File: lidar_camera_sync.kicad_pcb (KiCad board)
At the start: 2 copper layers, 64 parts, among them J1 SWD, J2 XLB16PW-M, J3 XLB16PW-M, J4 BM08B-GHS-TBT(LF)(SN), J5 Pinheader_4P, SW1 TS-1088-AR02016, U1 STM32G431KBUx, U2 TPS54560DDAR, U3 RT9013-33GB, U4 AMS1117-5.0, U5 MAX3232ESE+T, U6 ISO7720D, Y1 X32258MOB4SI

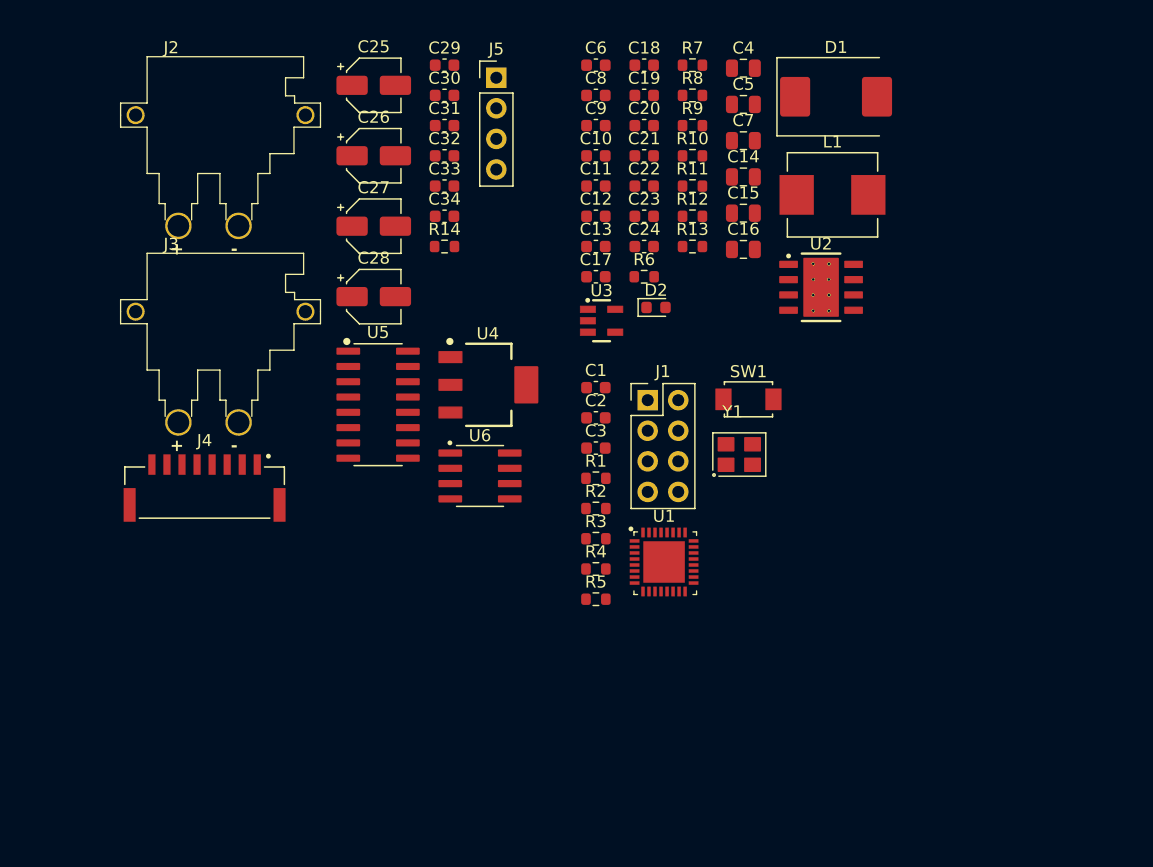
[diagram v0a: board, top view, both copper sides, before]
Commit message: [Modify]: 修复一些封装错误, 完成基本Layout器件摆放
JIRA-ID: N/A

修复一些封装错误, 完成基本Layout器件摆放
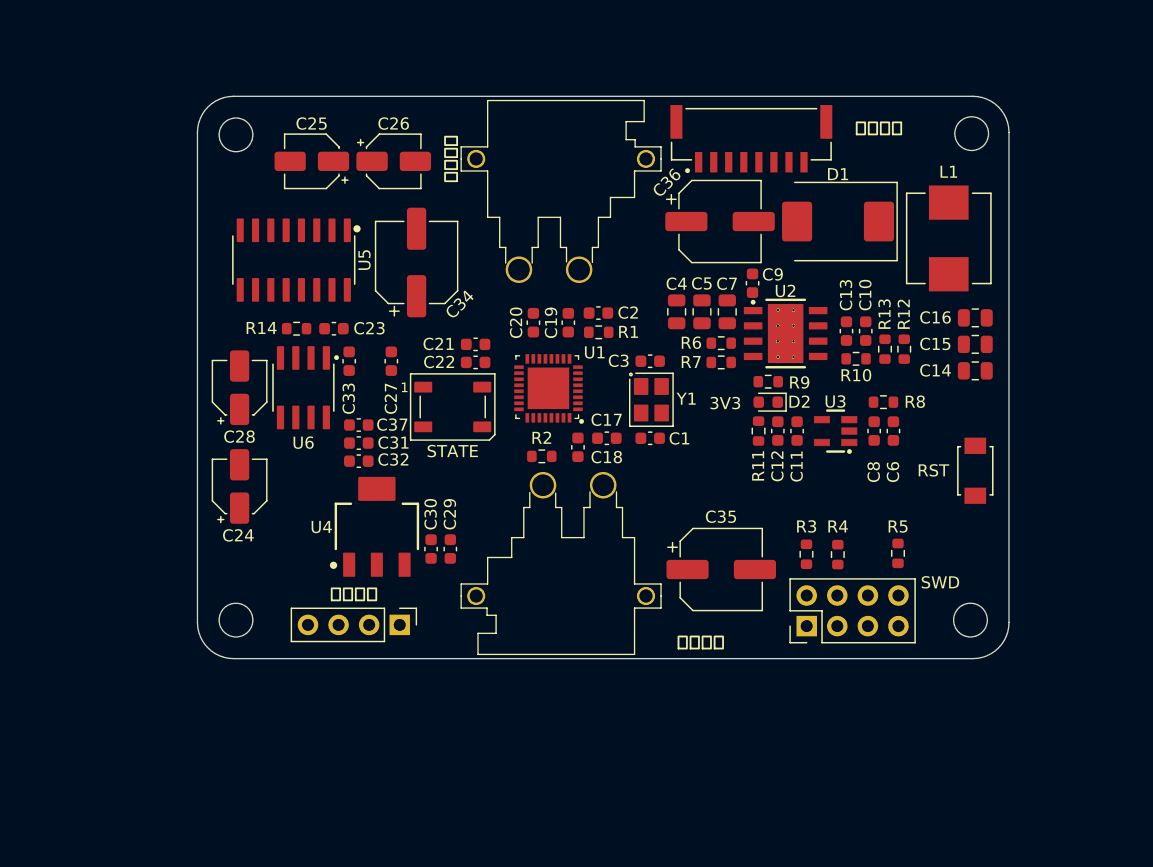
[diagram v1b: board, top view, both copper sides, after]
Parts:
- removed the C24 at (138.5, 94.4)
- added C27: 100nF, Capacitor_SMD:C_0603_1608Metric, F.Cu at (117.5, 103.9)
- added C34: 22uF, Capacitor_SMD:CP_Elec_6.3x5.4, F.Cu at (119.6, 95.7)
- added C35: 22uF, Capacitor_SMD:CP_Elec_6.3x5.4, F.Cu at (144.9, 121.2)
- added C36: 22uF, Capacitor_SMD:CP_Elec_6.3x5.4, F.Cu at (144.8, 92.3)
- added STATE: WS2812B, LED_SMD:LED_WS2812B_PLCC4_5.0x5.0mm_P3.2mm, F.Cu at (122.6, 107.7)
- SWD: renamed from J1; footprint Connector_PinHeader_2.54mm:PinHeader_2x04_P2.54mm_Vertical -> lidar_camera_sync:Pinheader_2x04_P2.54mm
- moved J4 55.4 mm to (147.4, 84.0), turned to 180 degrees
- moved 雷达接口 46.1 mm to (118.2, 125.8), turned to -90 degrees
- moved C29 40.2 mm to (122.4, 119.5), turned to 90 degrees
- moved C6 39.2 mm to (159.2, 109.7), turned to 90 degrees
- moved C30 37.7 mm to (120.8, 119.5), turned to 90 degrees
- moved 雷达电源 36.8 mm to (131.6, 123.4), turned to 180 degrees
- moved C8 36.2 mm to (157.6, 109.7), turned to 90 degrees
- moved C24 35.1 mm to (104.9, 114.3), turned to 90 degrees
- moved C18 32.2 mm to (133.0, 111.0), turned to -90 degrees
- moved R8 30.0 mm to (158.4, 107.3)
- moved 相机电源 28.5 mm to (131.6, 87.1)
- moved C23 27.4 mm to (112.7, 101.2), turned to 180 degrees
- moved C31 27.3 mm to (114.8, 110.7)
- moved C10 26.7 mm to (156.9, 101.4), turned to 90 degrees
- moved C32 26.3 mm to (114.8, 112.2)
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- renumbered C25 to C24, C26 to C25, C27 to C26, C34 to C37, SW1 to RST, J2 to 相机电源, J5 to 雷达接口, J3 to 雷达电源
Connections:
- U1 pad 18: unconnected-(U1-PA8-Pad18) -> /MCU/LED_DOUT
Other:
- board outline added: 67.4 x 46.7 mm
- board text added: "3V3"
- board text added: "相机同步"

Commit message: [New]: 完成PCB编辑以及DRC设计检查
JIRA-ID: N/A

完成PCB编辑以及DRC设计检查, 等待打板验证以及导出BOM表
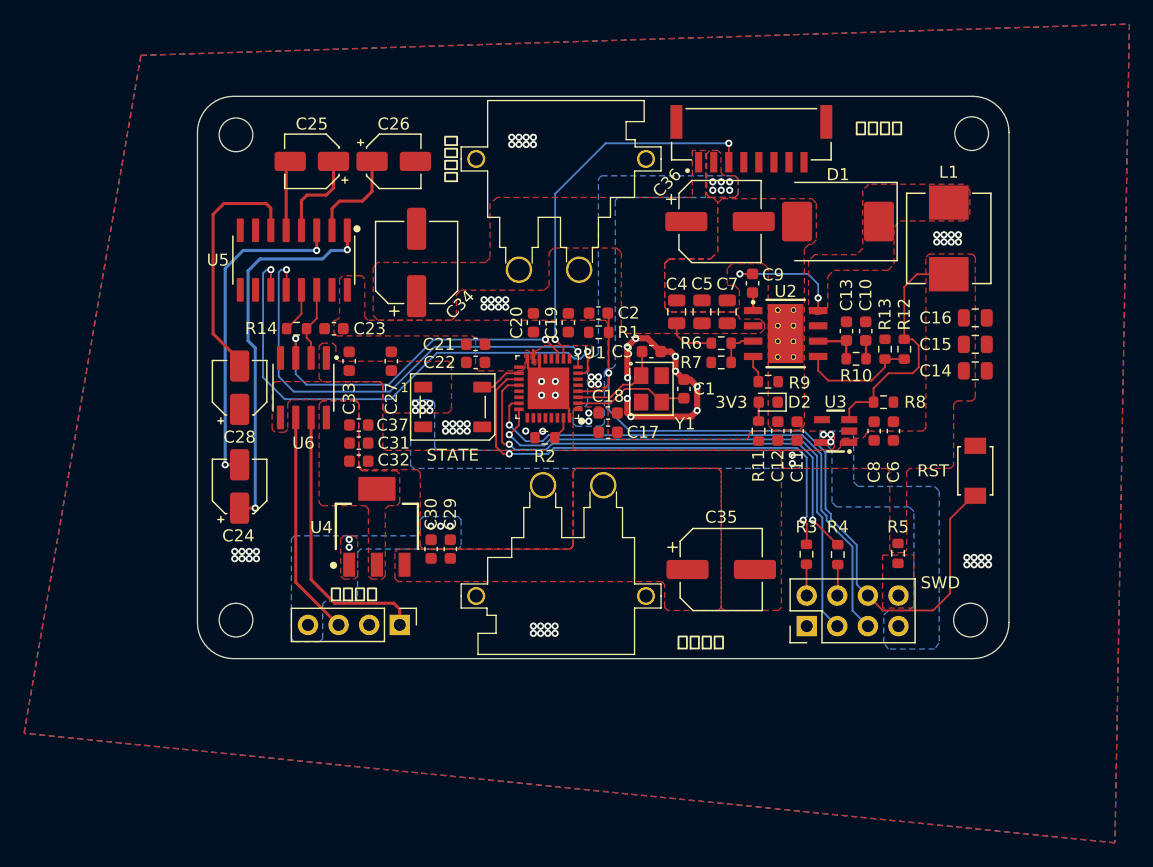
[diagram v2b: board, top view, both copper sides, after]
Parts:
- moved C1 4.96 mm to (141.8, 106.2), turned to 90 degrees
- moved C18 3.79 mm to (135.5, 108.2), turned to 0 degrees
- moved R2 1.57 mm to (130.2, 110.2)
- moved Y1 0.90 mm to (139.1, 106.2)
- moved C3 0.81 mm to (139.1, 103.1)
- moved C17 0.51 mm to (135.5, 109.8)
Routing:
- net /MCU/~{nRST}: track 0.00 -> 61.7 mm, vias 0 -> 1
- net /MCU/SWDIO: track 0.00 -> 45.7 mm, vias 0 -> 1
- net /MCU/SWCLK: track 0.00 -> 44.1 mm, vias 0 -> 1
- net /MCU/USART2_TXD: track 0.00 -> 43.3 mm, vias 0 -> 2
- net /MCU/USART1_TXD: track 0.00 -> 41.0 mm, vias 0 -> 2
- net /MCU/USART1_RXD: track 0.00 -> 40.9 mm, vias 0 -> 2
- net /MCU/USART2_RXD: track 0.00 -> 39.5 mm, vias 0 -> 2
- net /Peripheral/C1+: track 0.00 -> 31.8 mm, vias 0 -> 2
- net /MCU/PWM_CH2: track 0.00 -> 31.7 mm, vias 0 -> 2
- net /MCU/GND: track 0.00 -> 29.5 mm, vias 0 -> 71
- net /MCU/PWM_CH1: track 0.00 -> 29.2 mm, vias 0 -> 2
- net /Peripheral/C1-: track 0.00 -> 27.4 mm, vias 0 -> 2
- net Net-(J5-Pin_1): track 0.00 -> 23.2 mm
- net /Peripheral/V-: track 0.00 -> 20.7 mm
- net /Peripheral/VCC_5V0: track 0.00 -> 20.5 mm, vias 0 -> 8
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- added copper zone on F.Cu, net /MCU/5V0
- added copper zone on B.Cu, net /MCU/GND
- added copper zone on F.Cu, net /MCU/GND
- added copper zone on B.Cu, net /MCU/VCC_3V3
- added copper zone on F.Cu, net /MCU/VCC_3V3
- added copper zone on F.Cu, net /Peripheral/12V_CAMERA
- added copper zone on F.Cu, net /Peripheral/5V_LIDAR
- added copper zone on B.Cu, net /Peripheral/GND_LIDAR
- added copper zone on F.Cu, net /Peripheral/GND_LIDAR
- added copper zone on B.Cu, net /Peripheral/VCC_5V0
- added copper zone on F.Cu, net /Peripheral/VCC_5V0
- added copper zone on F.Cu, net /Peripheral/VDC_LIDAR
- added copper zone on F.Cu, net Net-(D1-K)

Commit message: [New]: 生成嘉立创打板文件和BOM表
JIRA-ID: N/A

生成嘉立创打板文件和BOM表
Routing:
- net /MCU/GND: track 29.5 -> 45.2 mm
- net /Peripheral/GND_LIDAR: track 0.00 -> 11.9 mm
- net /Peripheral/12V_CAMERA: track 4.13 -> 11.1 mm
- net /Peripheral/VDC_LIDAR: track 0.00 -> 6.54 mm
- net /MCU/VCC_3V3: track 0.74 -> 5.61 mm
